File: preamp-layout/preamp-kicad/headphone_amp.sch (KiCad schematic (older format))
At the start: 35 parts, among them J13 Conn_01x02_Male, J14 Conn_01x02_Female, J15 Conn_01x03_Male, J16 Conn_01x03_Female

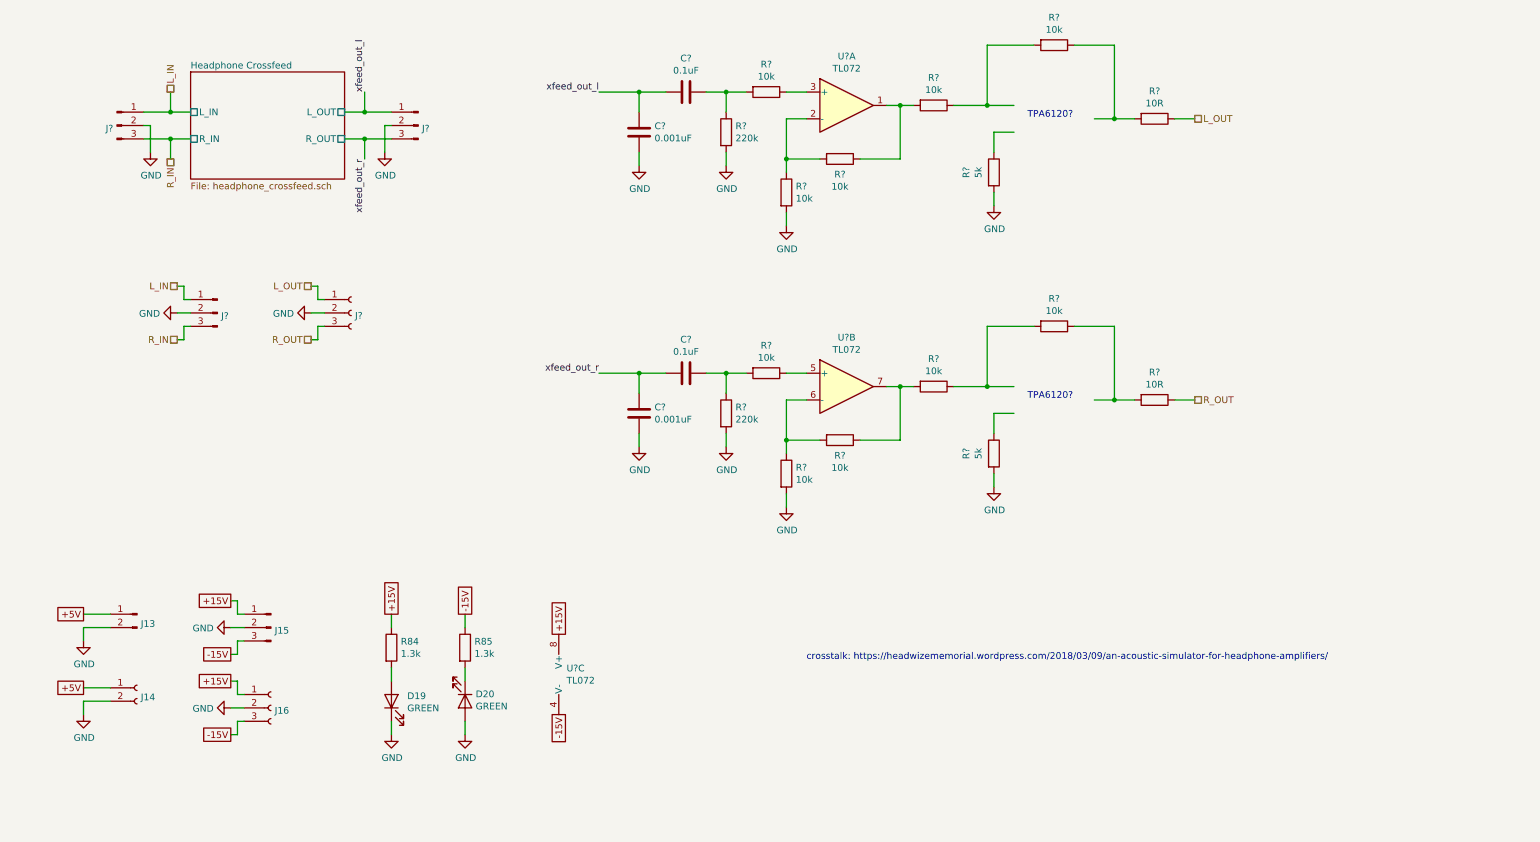
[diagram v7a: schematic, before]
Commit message: BOM Update
parts added to BOM, connector cleanup. Stopping point before renumbering refdes in a more intelligent way.
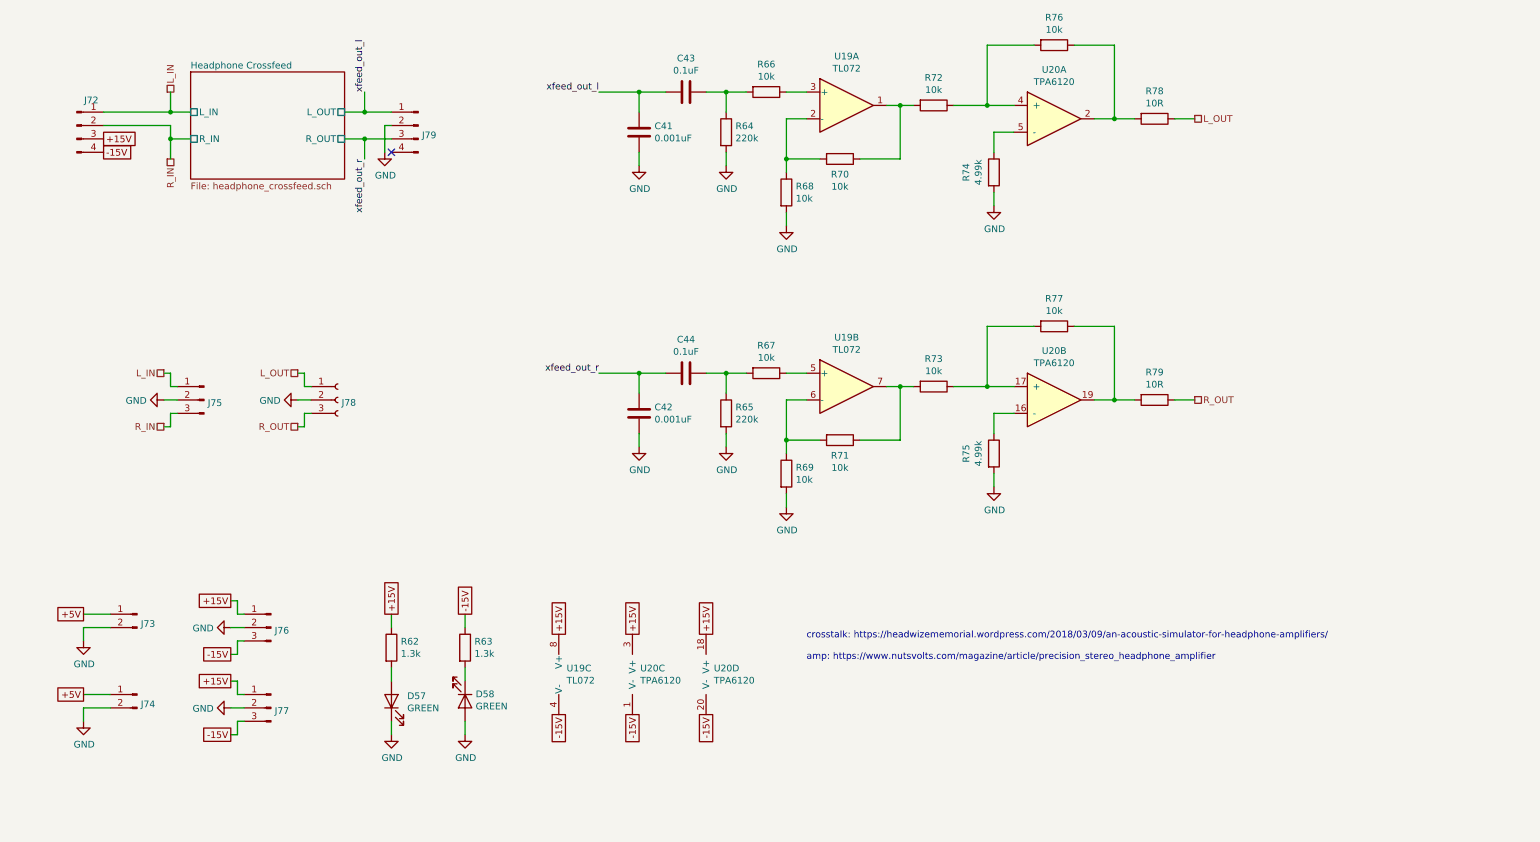
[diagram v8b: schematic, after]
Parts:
- removed J14: Conn_01x02_Female, symbol Connector:Conn_01x02_Female
- removed J16: Conn_01x03_Female, symbol Connector:Conn_01x03_Female
- removed J? (x2): Conn_01x03_Male, symbol Connector:Conn_01x03_Male
- added J72, J79: Conn_01x04_Male, symbol Connector:Conn_01x04_Male
- added J74: Conn_01x02_Male, Connector_JST:JST_EH_B2B-EH-A_1x02_P2.50mm_Vertical, symbol Connector:Conn_01x02_Male
- added J77: Conn_01x03_Male, Connector_JST:JST_EH_B3B-EH-A_1x03_P2.50mm_Vertical, symbol Connector:Conn_01x03_Male
- added U20: TPA6120, symbol preamp:TPA6120
- J73: renamed from J13; footprint (none) -> Connector_JST:JST_EH_B2B-EH-A_1x02_P2.50mm_Vertical
- J76: renamed from J15; footprint (none) -> Connector_JST:JST_EH_B3B-EH-A_1x03_P2.50mm_Vertical
- R74, R75: renamed from R?; value 5k -> 4.99k
- gave numbers to parts that had none: 21
- renumbered D19 to D57, D20 to D58, R84 to R62, R85 to R63
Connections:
- wire segments 116 -> 115
- no-connect marks 0 -> 1
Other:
- note added: "crosstalk: https://headwizememorial.wordpress.com/2018/03/09/an-acoustic-simulator-for-headphone-amplifiers/\n\namp: https://www.nutsvolts.com/magazine/article/precision_stereo_headphone_amplifier"
- note removed: "TPA6120?"
- note removed: "crosstalk: https://headwizememorial.wordpress.com/2018/03/09/an-acoustic-simulator-for-headphone-amplifiers/"
- moved on the sheet: J75, J78
